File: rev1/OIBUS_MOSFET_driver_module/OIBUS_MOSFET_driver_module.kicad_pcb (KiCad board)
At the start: 2 copper layers, 90.2 x 95.9 mm, 151 parts, among them J1 SWD, J10 +, J11 +, J12 +, J13 +, J2 UART, J3 5V - 24V, Molex Ultrafit, J4 +, J5 +, J6 +, J7 +, J8 +, J9 +, T1 DMG6402LVT, T10 DMG6402LVT, T2 DMG6402LVT, T3 DMG6402LVT, T4 DMG6402LVT, T5 DMG6402LVT, T6 DMG6402LVT, T7 DMG6402LVT, T8 DMG6402LVT, T9 DMG6402LVT, U1 TLP291, U10 STM32F303CCTx, U11 TLP291, U12 TLP291, U2 TLP291, U3 TLP291, U4 TLP291, U5 TLP291, U6 TLP291, U7 TLP291, U8 TLP291, U9 TCAN330, Y1 16M

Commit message: continuing layout
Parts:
- moved J8 112.4 mm to (56.8, 66.4), turned to 270 degrees
- moved JP19 107.8 mm to (68.6, 23.1)
- moved JP23 107.2 mm to (80.0, 18.8)
- moved JP27 106.8 mm to (61.5, 18.3)
- moved JP24 106.7 mm to (75.9, 18.5)
- moved JP16 105.3 mm to (56.1, 23.1)
- moved JP8 103.7 mm to (120.4, 23.6)
- moved JP25 103.3 mm to (71.1, 18.5)
- moved J9 98.0 mm to (56.8, 91.9), turned to 270 degrees
- moved JP20 97.7 mm to (72.4, 23.1)
- moved T6 95.0 mm to (60.8, 96.4), turned to 180 degrees
- moved JP15 92.2 mm to (52.3, 23.1)
- moved JP10 91.5 mm to (21.2, 65.3)
- moved J10 91.0 mm to (56.8, 117.3), turned to 270 degrees
- moved J13 89.4 mm to (56.8, 79.1), turned to 270 degrees
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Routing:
- added copper zone on F.Cu, net GNDPWR
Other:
- outline, holes or cut-outs redrawn

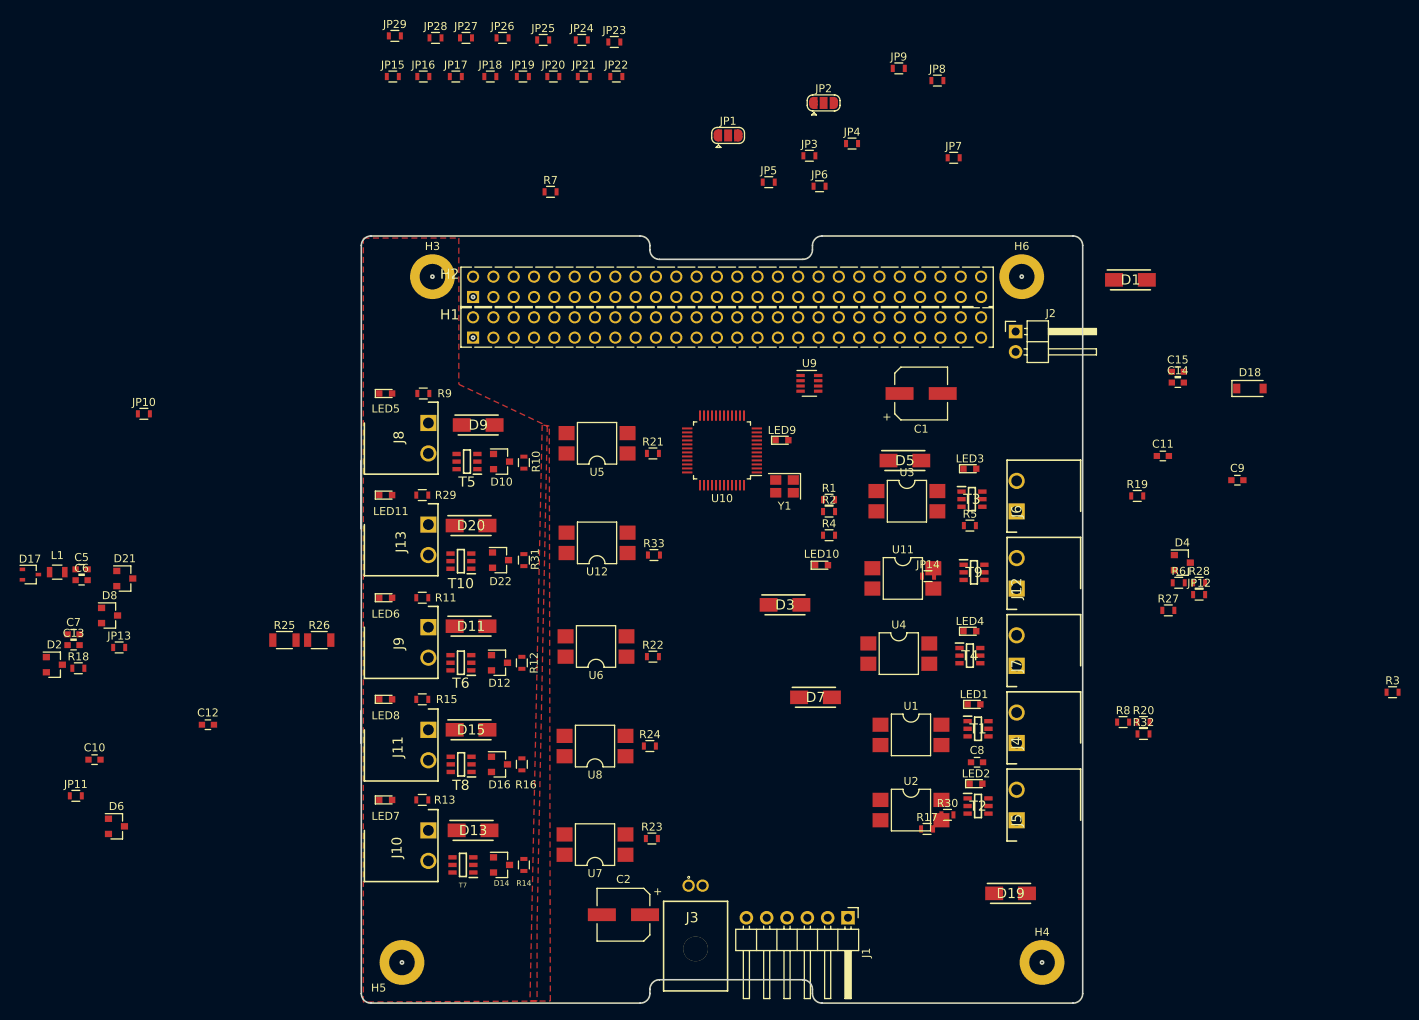
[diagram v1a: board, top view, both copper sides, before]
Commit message: adding power lanes
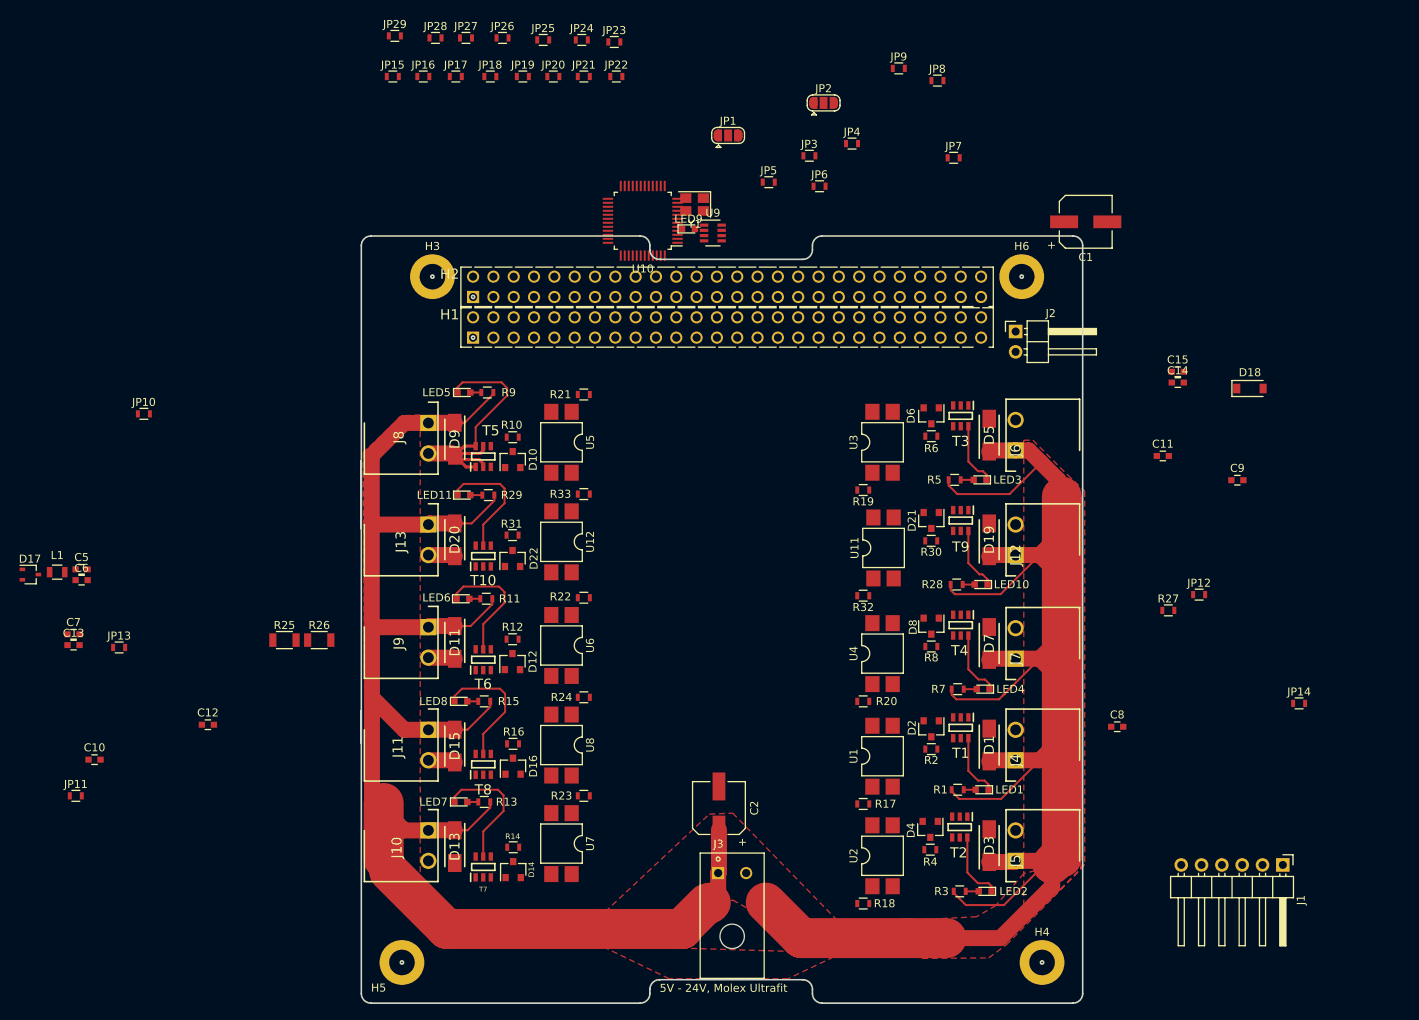
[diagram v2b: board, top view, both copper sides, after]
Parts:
- J3: footprint 172310-1202:172310-1202 -> 172310-1202:MOLEX_172310-1202
- moved D6 114.0 mm to (119.6, 65.5), turned to 270 degrees
- moved D2 109.9 mm to (119.6, 104.6), turned to 270 degrees
- moved D8 102.7 mm to (119.6, 91.8), turned to 270 degrees
- moved R18 102.4 mm to (111.1, 126.5), turned to 180 degrees
- moved D21 101.1 mm to (119.6, 78.6), turned to 270 degrees
- moved R7 80.3 mm to (122.9, 99.7), turned to 180 degrees
- moved D1 60.8 mm to (126.9, 106.7), turned to 90 degrees
- moved R3 59.6 mm to (123.2, 125.0), turned to 180 degrees
- moved J1 54.8 mm to (163.6, 121.7)
- moved JP14 49.0 mm to (165.6, 101.5)
- moved D4 45.9 mm to (119.5, 117.2), turned to 270 degrees
- moved D19 44.3 mm to (126.9, 81.0), turned to 90 degrees
- moved R4 41.3 mm to (119.5, 119.8)
- moved R1 39.7 mm to (122.9, 112.3), turned to 180 degrees
- moved D3 39.5 mm to (126.9, 119.3), turned to 90 degrees
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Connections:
- J10 pad 2: Net-(J10-Pad2) -> Net-(D13-Pad2)
- J11 pad 2: Net-(J11-Pad2) -> Net-(D15-Pad2)
- J12 pad 2: Net-(J12-Pad2) -> Net-(D19-Pad2)
- J13 pad 2: Net-(J13-Pad2) -> Net-(D20-Pad2)
- J4 pad 2: Net-(J4-Pad2) -> Net-(D1-Pad2)
- J5 pad 2: Net-(J5-Pad2) -> Net-(D3-Pad2)
- J6 pad 2: Net-(J6-Pad2) -> Net-(D5-Pad2)
- J7 pad 2: Net-(J7-Pad2) -> Net-(D7-Pad2)
- J8 pad 2: Net-(J8-Pad2) -> Net-(D9-Pad2)
- J9 pad 2: Net-(J9-Pad2) -> Net-(D11-Pad2)
- T1 pad 5: Net-(J4-Pad2) -> Net-(D1-Pad2)
- T1 pad 6: Net-(J4-Pad2) -> Net-(D1-Pad2)
- T10 pad 5: Net-(J13-Pad2) -> Net-(D20-Pad2)
- T10 pad 6: Net-(J13-Pad2) -> Net-(D20-Pad2)
- T2 pad 5: Net-(J5-Pad2) -> Net-(D3-Pad2)
- T2 pad 6: Net-(J5-Pad2) -> Net-(D3-Pad2)
- T3 pad 5: Net-(J6-Pad2) -> Net-(D5-Pad2)
- T3 pad 6: Net-(J6-Pad2) -> Net-(D5-Pad2)
- T4 pad 5: Net-(J7-Pad2) -> Net-(D7-Pad2)
- T4 pad 6: Net-(J7-Pad2) -> Net-(D7-Pad2)
- T5 pad 5: Net-(J8-Pad2) -> Net-(D9-Pad2)
- T5 pad 6: Net-(J8-Pad2) -> Net-(D9-Pad2)
- T6 pad 5: Net-(J9-Pad2) -> Net-(D11-Pad2)
- T6 pad 6: Net-(J9-Pad2) -> Net-(D11-Pad2)
- T7 pad 5: Net-(J10-Pad2) -> Net-(D13-Pad2)
- T7 pad 6: Net-(J10-Pad2) -> Net-(D13-Pad2)
- T8 pad 5: Net-(J11-Pad2) -> Net-(D15-Pad2)
- T8 pad 6: Net-(J11-Pad2) -> Net-(D15-Pad2)
- T9 pad 5: Net-(J12-Pad2) -> Net-(D19-Pad2)
- T9 pad 6: Net-(J12-Pad2) -> Net-(D19-Pad2)
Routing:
- net VBUS: track 0.00 -> 443.0 mm
- net Net-(D9-Pad2): track 0.00 -> 34.5 mm
- net Net-(D15-Pad2): track 0.00 -> 19.7 mm
- net Net-(D11-Pad2): track 0.00 -> 18.9 mm
- net Net-(D20-Pad2): track 0.00 -> 18.7 mm
- net Net-(D13-Pad2): track 0.00 -> 16.1 mm
- net Net-(D3-Pad2): track 0.00 -> 8.76 mm
- net Net-(D7-Pad2): track 0.00 -> 8.27 mm
- net Net-(D5-Pad2): track 0.00 -> 8.00 mm
- net Net-(D1-Pad2): track 0.00 -> 7.97 mm
- net Net-(D19-Pad2): track 0.00 -> 7.91 mm
- net Net-(LED4-Pad2): track 0.00 -> 1.62 mm
- net Net-(LED3-Pad2): track 0.00 -> 1.62 mm
- net Net-(LED2-Pad2): track 0.00 -> 1.62 mm
- net Net-(LED10-Pad2): track 0.00 -> 1.50 mm
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- added copper zone on F.Cu, net VBUS
- removed copper zone on F.Cu, net GNDPWR
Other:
- net class Analog added: clearance 0.2, trace_width 0.25, via_dia 0.7, via_drill 0.4
- net class Default: trace_width 0.25 -> 0.2; via_dia 0.8 -> 0.6; via_drill 0.4 -> 0.3
- net class HighCurrent added: clearance 1, trace_width 2, via_dia 1, via_drill 0.6
- net class HighCurrent2 added: clearance 1, trace_width 5, via_dia 1, via_drill 0.6
- net class Power added: clearance 0.25, trace_width 0.4, via_dia 1, via_drill 0.6

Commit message: pcb layout completed and ready for review
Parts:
- removed JP13, JP14, JP15, JP16, JP17, JP18, JP19, JP20, JP4, JP6, JP7, JP8: SolderJumper_2_Open, Resistors_SMD:R_0603
- moved J1 126.2 mm to (52.6, 61.6), turned to 180 degrees
- moved JP28 99.7 mm to (101.5, 107.8), turned to 270 degrees
- moved D17 94.0 mm to (97.2, 58.5), turned to 180 degrees
- moved L1 91.1 mm to (100.1, 100.8), turned to 180 degrees
- moved C13 88.2 mm to (100.6, 91.8), turned to 180 degrees
- moved R27 87.8 mm to (73.7, 45.2), turned to 180 degrees
- moved JP11 87.3 mm to (84.2, 62.9), turned to 270 degrees
- moved C7 84.3 mm to (95.8, 105.3), turned to 90 degrees
- moved C1 82.4 mm to (101.6, 114.7), turned to 180 degrees
- moved C5 81.0 mm to (92.3, 66.4), turned to 270 degrees
- moved D18 80.9 mm to (102.6, 119.6), turned to 180 degrees
- moved C6 75.7 mm to (88.3, 74.7), turned to 90 degrees
- moved C10 71.7 mm to (86.2, 99.8)
- moved JP12 71.5 mm to (86.1, 62.9), turned to 270 degrees
- moved J2 71.4 mm to (108.0, 122.8), turned to 270 degrees
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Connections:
- H2 pad 29: Net-(H2-Pad29) -> GND
- H2 pad 30: Net-(H2-Pad29) -> GND
- H3 pad 1: GNDPWR -> GND
- H4 pad 1: GNDPWR -> GND
- H5 pad 1: GNDPWR -> GND
- H6 pad 1: GNDPWR -> GND
- JP1 pad 1: Tx -> Net-(H1-Pad39)
- JP1 pad 3: Net-(H1-Pad39) -> Tx
- JP28 pad 1: Net-(H2-Pad29) -> GND
- JP5 pad 2: ADC2 -> ADC1
- U10 pad 12: ADC1 -> Net-(U10-Pad12)
- U10 pad 14: ADC2 -> ADC1
- U10 pad 15: ADC3 -> Net-(U10-Pad15)
- U10 pad 16: ADC4 -> Net-(U10-Pad16)
- U10 pad 17: ADC5 -> Net-(U10-Pad17)
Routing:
- net GND: track 0.00 -> 385.8 mm, vias 0 -> 28
- net Vopto: track 0.00 -> 190.6 mm
- net +3V3: track 0.00 -> 176.1 mm, vias 0 -> 7
- net VBUS: track 443.0 -> 565.6 mm, vias 0 -> 4
- net ~RESET: track 0.00 -> 117.5 mm, vias 0 -> 4
- net Net-(R27-Pad2): track 0.00 -> 95.5 mm, vias 0 -> 4
- net Net-(H1-Pad47): track 0.00 -> 89.9 mm, vias 0 -> 8
- net VBACKUP: track 0.00 -> 86.3 mm, vias 0 -> 5
- net Net-(H1-Pad39): track 0.00 -> 79.4 mm, vias 0 -> 4
- net ADC1: track 0.00 -> 76.6 mm, vias 0 -> 4
- net GNDPWR: track 0.00 -> 74.8 mm, vias 0 -> 22
- net SWDSWO: track 0.00 -> 69.3 mm, vias 0 -> 3
- net SWDCLK: track 0.00 -> 68.0 mm, vias 0 -> 1
- net SWDIO: track 0.00 -> 64.4 mm, vias 0 -> 3
- net GPIO1: track 0.00 -> 56.2 mm, vias 0 -> 2
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- added copper zone on B.Cu, net GND
- added copper zone on B.Cu, net GNDPWR
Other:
- outline, holes or cut-outs redrawn
- board text added: "OIBUS MOSFET driver Revision 1, 2018, SS Octanis Instruments OÜ"
